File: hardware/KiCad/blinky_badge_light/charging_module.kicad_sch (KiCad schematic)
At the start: 17 parts, among them Q1 N-Channel MOSFET, Q3 N-Channel MOSFET, Q4 Q_PMOS_GSD, U2 TP4056

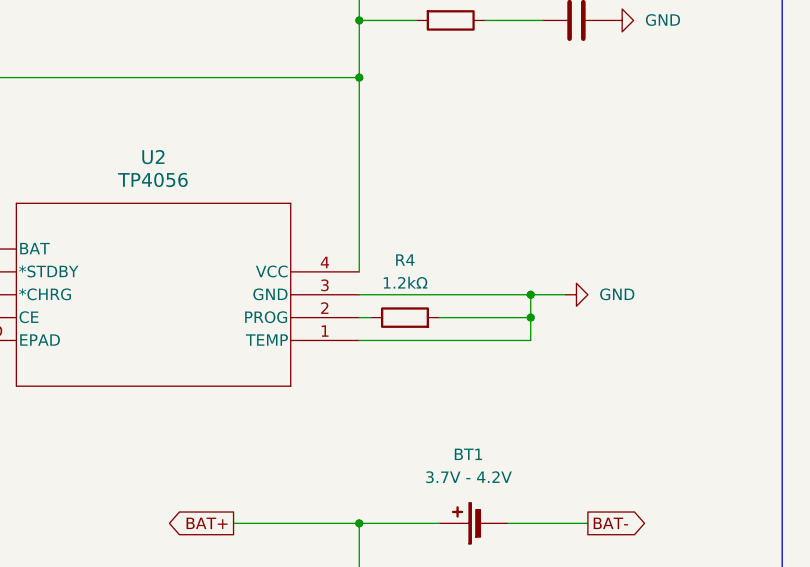
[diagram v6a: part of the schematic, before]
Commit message: change charging prog resistor to 2k to keep things cooler
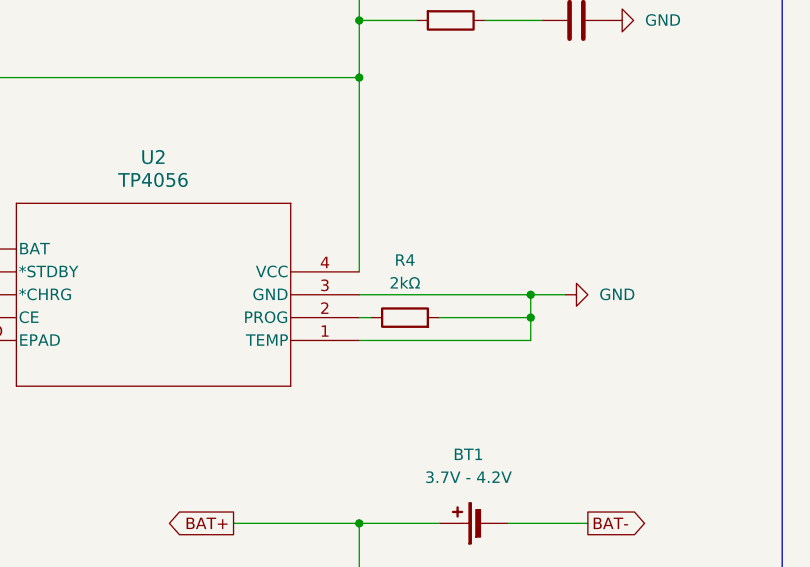
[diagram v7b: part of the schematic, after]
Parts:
- R4: value 1.2kΩ -> 2kΩ; JLCPCB Part # C22764 -> C22975
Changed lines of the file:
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@@
 			)
 		)
-		(property "Value" "1.2kΩ"
+		(property "Value" "2kΩ"
 			(at 111.76 83.82 90)
 			(effects
@@
 			)
 		)
-		(property "Datasheet" "https://jlcpcb.com/api/file/downloadByFileSystemAccessId/8579706389601501184"
+		(property "Datasheet" "https://jlcpcb.com/api/file/downloadByFileSystemAccessId/8579706189568917504"
 			(at 111.76 87.63 0)
 			(effects
@@
 			)
 		)
-		(property "JLCPCB Part #" "C22764"
+		(property "JLCPCB Part #" "C22975"
 			(at 111.76 87.63 90)
 			(effects

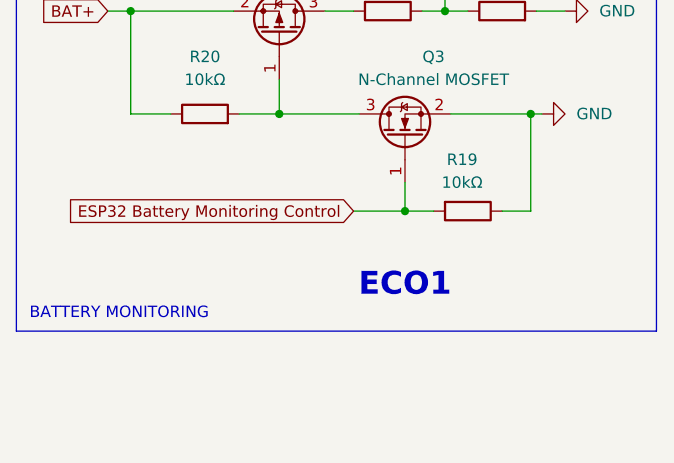
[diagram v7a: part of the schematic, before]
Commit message: remove comment from schematic
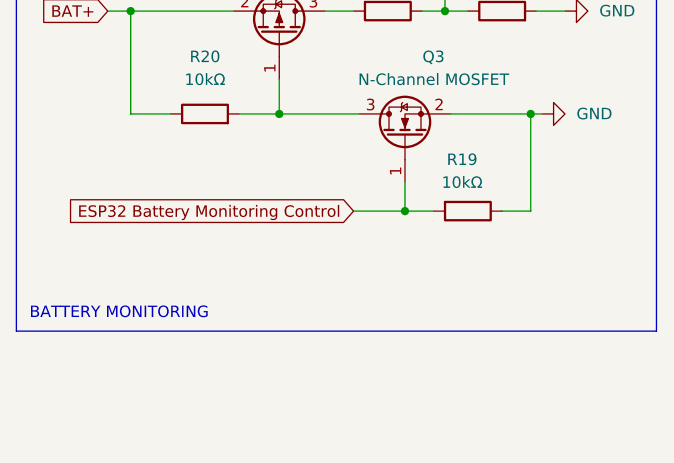
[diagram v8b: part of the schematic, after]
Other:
- note removed: "ECO1"
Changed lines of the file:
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@@
-		)
-	)
-	(text "ECO1"
-		(exclude_from_sim yes)
-		(at 200.66 115.57 0)
-		(effects
-			(font
-				(face "KiCad Font")
-				(size 2.54 2.54)
-				(thickness 0.508)
-				(bold yes)
-				(color 137 36 255 1)
-			)
 		)
 	)
